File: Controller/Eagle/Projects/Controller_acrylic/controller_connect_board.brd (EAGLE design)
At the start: 280.8 x 115 mm, 17 parts, among them J1 GIMBAL_3PIN, J2 GIMBAL_3PIN, J3 GIMBAL_3PIN, J4 GIMBAL_3PIN

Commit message: Made new eagle project for controller connector board Made new JST connect device that matches the JST connector (not sure why it didn't originally)
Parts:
- added J5: GIMBAL_3PIN_MATCH_TDOCU, Controller:JST-3-PTH
- added JP2: (no value), SparkFun-Connectors:1X01
- J1, J2, J3, J4: value GIMBAL_3PIN -> GIMBAL_3PIN_MATCH_TDOCU
- R1, R2, R3, R4: value (none) -> 5k
- moved R1 47.7 mm to (108.3, 38.2), turned to 270 degrees
- moved U$3 46.1 mm to (123.9, 114.0), flipped to the top
- moved J4 43.4 mm to (83.0, 49.0), turned to 270 degrees
- moved J2 17.7 mm to (200.0, 28.0)
- moved R3 16.6 mm to (187.4, 33.0), turned to 180 degrees
- moved R2 9.22 mm to (70.9, 37.9)
- moved R4 8.54 mm to (172.6, 40.7)
- moved U$6 8.54 mm to (98.0, 33.0)
- moved U$7 8.54 mm to (153.0, 33.0)
- moved JP1 8.25 mm to (105.0, 52.0), turned to 270 degrees
- moved J1 6.71 mm to (186.0, 51.0)
- moved J3 6.08 mm to (71.0, 49.0)
- moved JP6 2.24 mm to (126.0, 45.0)
- turned U$1 to 180 degrees
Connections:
- new net N$9: J5.3, JP2.1
- net 3.3V: now also J5.1
- net GND: now also J1.2, J2.2, J3.2, J4.2, J5.2; no longer J1.3, J2.3, J3.3, J4.3
- net N$5: now also J1.3; no longer J1.2
- net N$6: now also J2.3; no longer J2.2
- net N$7: now also J3.3; no longer J3.2
- net N$8: now also J4.3; no longer J4.2
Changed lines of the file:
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@@
 <layer number="49" name="Reference" color="7" fill="1" visible="no" active="yes"/>
 <layer number="50" name="dxf" color="7" fill="1" visible="no" active="no"/>
-<layer number="51" name="tDocu" color="7" fill="1" visible="no" active="yes"/>
-<layer number="52" name="bDocu" color="7" fill="1" visible="no" active="yes"/>
+<layer number="51" name="tDocu" color="7" fill="1" visible="yes" active="yes"/>
+<layer number="52" name="bDocu" color="7" fill="1" visible="yes" active="yes"/>
 <layer number="53" name="tGND_GNDA" color="7" fill="1" visible="no" active="no"/>
 <layer number="54" name="bGND_GNDA" color="7" fill="1" visible="no" active="no"/>
@@
 <dimension x1="220" y1="57.5" x2="220" y2="0" x3="206.3" y3="28.75" textsize="1.778" layer="47" visible="yes"/>
 <dimension x1="220" y1="57.5" x2="250" y2="61.6" x3="235" y3="62.85" textsize="1.778" layer="47" dtype="horizontal" visible="yes"/>
+<wire x1="217" y1="22" x2="217" y2="44" width="0.01" layer="20"/>
+<wire x1="217" y1="44" x2="190" y2="44" width="0.01" layer="20"/>
+<wire x1="190" y1="44" x2="190" y2="55" width="0.01" layer="20"/>
+<wire x1="190" y1="55" x2="67" y2="55" width="0.01" layer="20"/>
+<wire x1="67" y1="55" x2="67" y2="42" width="0.01" layer="20"/>
+<wire x1="67" y1="42" x2="32" y2="42" width="0.01" layer="20"/>
+<wire x1="32" y1="42" x2="32" y2="22" width="0.01" layer="20"/>
+<wire x1="32" y1="22" x2="217" y2="22" width="0.01" layer="20"/>
 </plain>
 <attributes>
@@
 </autorouter>
 <elements>
-<element name="U$3" library="BOBs" package="ATMEGA128RFA1" value="" x="170" y="114" rot="MR270"/>
-<element name="U$1" library="Controller" package="GIMBAL_FOOTPRINT" value="" x="29" y="72.5"/>
+<element name="U$3" library="BOBs" package="ATMEGA128RFA1" value="" x="123.883" y="113.963" rot="R270"/>
+<element name="U$1" library="Controller" package="GIMBAL_FOOTPRINT" value="" x="29" y="72.5" rot="R180"/>
 <element name="U$2" library="Controller" package="GIMBAL_FOOTPRINT" value="" x="221" y="72.5"/>
 <element name="U$4" library="Controller" package="SPARKFUN_LCD_33" value="" x="83" y="1"/>
 <element name="U$5" library="Controller" package="CONTROLLER_OUTLINE" value="" x="0" y="0"/>
-<element name="J1" library="Controller" package="JST-3-PTH" value="GIMBAL_3PIN" x="189" y="57" rot="R90"/>
-<element name="J2" library="Controller" package="JST-3-PTH" value="GIMBAL_3PIN" x="213" y="40" rot="R180"/>
-<element name="J3" library="Controller" package="JST-3-PTH" value="GIMBAL_3PIN" x="70" y="55" rot="R270"/>
-<element name="J4" library="Controller" package="JST-3-PTH" value="GIMBAL_3PIN" x="41" y="38" rot="R180"/>
-<element name="R1" library="SparkFun-Resistors" package="1/6W-RES" value="" x="60.780953125" y="42.318003125"/>
-<element name="R2" library="SparkFun-Resistors" package="1/6W-RES" value="" x="72.949403125" y="46.939940625"/>
-<element name="R3" library="SparkFun-Resistors" package="1/6W-RES" value="" x="201.042509375" y="42.352325" rot="R270"/>
-<element name="R4" library="SparkFun-Resistors" package="1/6W-RES" value="" x="175.58266875" y="48.739028125" rot="R270"/>
-<element name="JP6" library="SparkFun-Connectors" package="1X04" value="" x="124" y="46" rot="R90"/>
-<element name="JP1" library="SparkFun-Connectors" package="1X02_NO_SILK" value="" x="113" y="54" rot="R180"/>
-<element name="U$6" library="Components" package="FACEPLATE_MOUNTINGHOLE_M2.5_UNPLATED" value="" x="101" y="41"/>
-<element name="U$7" library="Components" package="FACEPLATE_MOUNTINGHOLE_M2.5_UNPLATED" value="" x="156" y="41"/>
+<element name="J1" library="Controller" package="JST-3-PTH" value="GIMBAL_3PIN_MATCH_TDOCU" x="186" y="51" rot="R90"/>
+<element name="J2" library="Controller" package="JST-3-PTH" value="GIMBAL_3PIN_MATCH_TDOCU" x="200" y="28" rot="R180"/>
+<element name="J3" library="Controller" package="JST-3-PTH" value="GIMBAL_3PIN_MATCH_TDOCU" x="71" y="49" rot="R270"/>
+<element name="J4" library="Controller" package="JST-3-PTH" value="GIMBAL_3PIN_MATCH_TDOCU" x="83" y="49" rot="R270"/>
+<element name="R1" library="SparkFun-Resistors" package="1/6W-RES" value="5k" x="108.318003125" y="38.219046875" rot="R270"/>
+<element name="R2" library="SparkFun-Resistors" package="1/6W-RES" value="5k" x="70.949403125" y="37.939940625"/>
+<element name="R3" library="SparkFun-Resistors" package="1/6W-RES" value="5k" x="187.352325" y="32.957490625" rot="R180"/>
+<element name="R4" library="SparkFun-Resistors" package="1/6W-RES" value="5k" x="172.58266875" y="40.739028125" rot="R270"/>
+<element name="JP6" library="SparkFun-Connectors" package="1X04" value="" x="126" y="45" rot="R90"/>
+<element name="JP1" library="SparkFun-Connectors" package="1X02_NO_SILK" value="" x="105" y="52" rot="R270"/>
+<element name="U$6" library="Components" package="FACEPLATE_MOUNTINGHOLE_M2.5_UNPLATED" value="" x="98" y="33"/>
+<element name="U$7" library="Components" package="FACEPLATE_MOUNTINGHOLE_M2.5_UNPLATED" value="" x="153" y="33"/>
+<element name="J5" library="Controller" package="JST-3-PTH" value="GIMBAL_3PIN_MATCH_TDOCU" x="133" y="29" rot="MR90"/>
+<element name="JP2" library="SparkFun-Connectors" package="1X01" value="" x="169" y="52"/>
 </elements>
 <signals>
 <signal name="GND">
-<contactref element="J4" pad="3"/>
-<contactref element="J1" pad="3"/>
-<contactref element="J2" pad="3"/>
-<contactref element="J3" pad="3"/>
+<contactref element="J4" pad="2"/>
+<contactref element="J1" pad="2"/>
+<contactref element="J2" pad="2"/>
+<contactref element="J3" pad="2"/>
 <contactref element="JP1" pad="1"/>
-<wire x1="211" y1="40" x2="189" y2="59" width="0" layer="19" extent="1-1"/>
-<wire x1="113" y1="54" x2="189" y2="59" width="0" layer="19" extent="1-1"/>
-<wire x1="70" y1="53" x2="113" y2="54" width="0" layer="19" extent="1-1"/>
-<wire x1="39" y1="38" x2="70" y2="53" width="0" layer="19" extent="1-1"/>
+<contactref element="J5" pad="2"/>
+<wire x1="186" y1="51" x2="200" y2="28" width="0" layer="19" extent="1-1"/>
+<wire x1="105" y1="52" x2="186" y2="51" width="0" layer="19" extent="1-1"/>
+<wire x1="71" y1="49" x2="105" y2="52" width="0" layer="19" extent="1-1"/>
+<wire x1="83" y1="49" x2="71" y2="49" width="0" layer="19" extent="1-1"/>
+<wire x1="133" y1="29" x2="83" y2="49" width="0" layer="19" extent="1-1"/>
 </signal>
 <signal name="N$1">
 <contactref element="J4" pad="1"/>
 <contactref element="R1" pad="1"/>
-<wire x1="43" y1="38" x2="58.280953125" y2="42.318003125" width="0" layer="19" extent="1-1"/>
+<wire x1="83" y1="51" x2="108.318003125" y2="40.719046875" width="0" layer="19" extent="1-1"/>
 </signal>
 <signal name="N$2">
 <contactref element="J3" pad="1"/>
 <contactref element="R2" pad="1"/>
-<wire x1="70.449403125" y1="46.939940625" x2="70" y2="57" width="0" layer="19" extent="1-1"/>
+<wire x1="68.449403125" y1="37.939940625" x2="71" y2="51" width="0" layer="19" extent="1-1"/>
 </signal>
 <signal name="N$3">
 <contactref element="J2" pad="1"/>
 <contactref element="R3" pad="1"/>
-<wire x1="201.042509375" y1="44.852325" x2="215" y2="40" width="0" layer="19" extent="1-1"/>
+<wire x1="189.852325" y1="32.957490625" x2="202" y2="28" width="0" layer="19" extent="1-1"/>
 </signal>
 <signal name="N$4">
 <contactref element="J1" pad="1"/>
 <contactref element="R4" pad="1"/>
-<wire x1="175.58266875" y1="51.239028125" x2="189" y2="55" width="0" layer="19" extent="1-1"/>
+<wire x1="172.58266875" y1="43.239028125" x2="186" y2="49" width="0" layer="19" extent="1-1"/>
 </signal>
 <signal name="3.3V">
@@
 <contactref element="R1" pad="2"/>
 <contactref element="JP1" pad="2"/>
-<wire x1="175.58266875" y1="46.239028125" x2="201.042509375" y2="39.852325" width="0" layer="19" extent="1-1"/>
-<wire x1="110.46" y1="54" x2="175.58266875" y2="46.239028125" width="0" layer="19" extent="1-1"/>
-<wire x1="75.449403125" y1="46.939940625" x2="110.46" y2="54" width="0" layer="19" extent="1-1"/>
-<wire x1="63.280953125" y1="42.318003125" x2="75.449403125" y2="46.939940625" width="0" layer="19" extent="1-1"/>
+<contactref element="J5" pad="1"/>
+<wire x1="172.58266875" y1="38.239028125" x2="184.852325" y2="32.957490625" width="0" layer="19" extent="1-1"/>
+<wire x1="105" y1="49.46" x2="172.58266875" y2="38.239028125" width="0" layer="19" extent="1-1"/>
+<wire x1="73.449403125" y1="37.939940625" x2="105" y2="49.46" width="0" layer="19" extent="1-1"/>
+<wire x1="108.318003125" y1="35.719046875" x2="73.449403125" y2="37.939940625" width="0" layer="19" extent="1-1"/>
+<wire x1="133" y1="27" x2="108.318003125" y2="35.719046875" width="0" layer="19" extent="1-1"/>
 </signal>
 <signal name="N$5">
-<contactref element="J1" pad="2"/>
+<contactref element="J1" pad="3"/>
 <contactref element="JP6" pad="1"/>
-<wire x1="124" y1="46" x2="189" y2="57" width="0" layer="19" extent="1-1"/>
+<wire x1="126" y1="45" x2="186" y2="53" width="0" layer="19" extent="1-1"/>
 </signal>
 <signal name="N$6">
-<contactref element="J2" pad="2"/>
+<contactref element="J2" pad="3"/>
 <contactref element="JP6" pad="2"/>
-<wire x1="124" y1="48.54" x2="213" y2="40" width="0" layer="19" extent="1-1"/>
+<wire x1="126" y1="47.54" x2="198" y2="28" width="0" layer="19" extent="1-1"/>
 </signal>
 <signal name="N$7">
-<contactref element="J3" pad="2"/>
+<contactref element="J3" pad="3"/>
 <contactref element="JP6" pad="3"/>
-<wire x1="70" y1="55" x2="124" y2="51.08" width="0" layer="19" extent="1-1"/>
+<wire x1="71" y1="47" x2="126" y2="50.08" width="0" layer="19" extent="1-1"/>
 </signal>
 <signal name="N$8">
-<contactref element="J4" pad="2"/>
+<contactref element="J4" pad="3"/>
 <contactref element="JP6" pad="4"/>
-<wire x1="41" y1="38" x2="124" y2="53.62" width="0" layer="19" extent="1-1"/>
+<wire x1="83" y1="47" x2="126" y2="52.62" width="0" layer="19" extent="1-1"/>
+</signal>
+<signal name="N$9">
+<contactref element="J5" pad="3"/>
+<contactref element="JP2" pad="1"/>
+<wire x1="133" y1="31" x2="169" y2="52" width="0" layer="19" extent="1-1"/>
 </signal>
 </signals>

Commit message: Routing and rubouts
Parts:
- removed U$1, U$2: (no value), Controller:GIMBAL_FOOTPRINT
- removed U$3: (no value), BOBs:ATMEGA128RFA1
- removed U$4: (no value), Controller:SPARKFUN_LCD_33
- removed U$5: (no value), Controller:CONTROLLER_OUTLINE
- moved J5 2.00 mm to (133.0, 27.0)
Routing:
- net GND: track 0.00 -> 224.4 mm
- net 3.3V: track 0.00 -> 174.7 mm
- net N$9: track 0.00 -> 89.0 mm
- net N$6: track 0.00 -> 80.1 mm, vias 0 -> 2
- net N$1: track 0.00 -> 72.5 mm
- net N$5: track 0.00 -> 63.5 mm
- net N$7: track 0.00 -> 57.4 mm
- net N$8: track 0.00 -> 45.4 mm
- net N$4: track 0.00 -> 15.8 mm
- net N$3: track 0.00 -> 14.2 mm
- net N$2: track 0.00 -> 14.1 mm
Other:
- board size 280.8 x 115 mm -> 185 x 33 mm

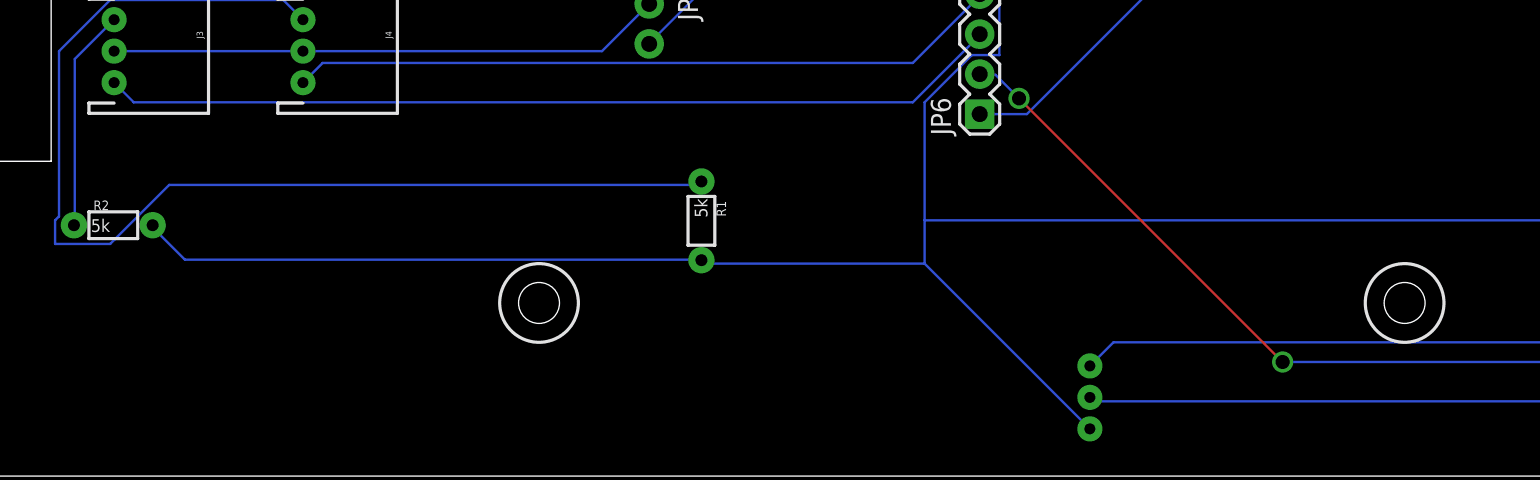
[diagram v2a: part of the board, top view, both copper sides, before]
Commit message: Controller connect board has only the board, no acrylic stuff Added connector board to library so it matches up with acrylic cutouts
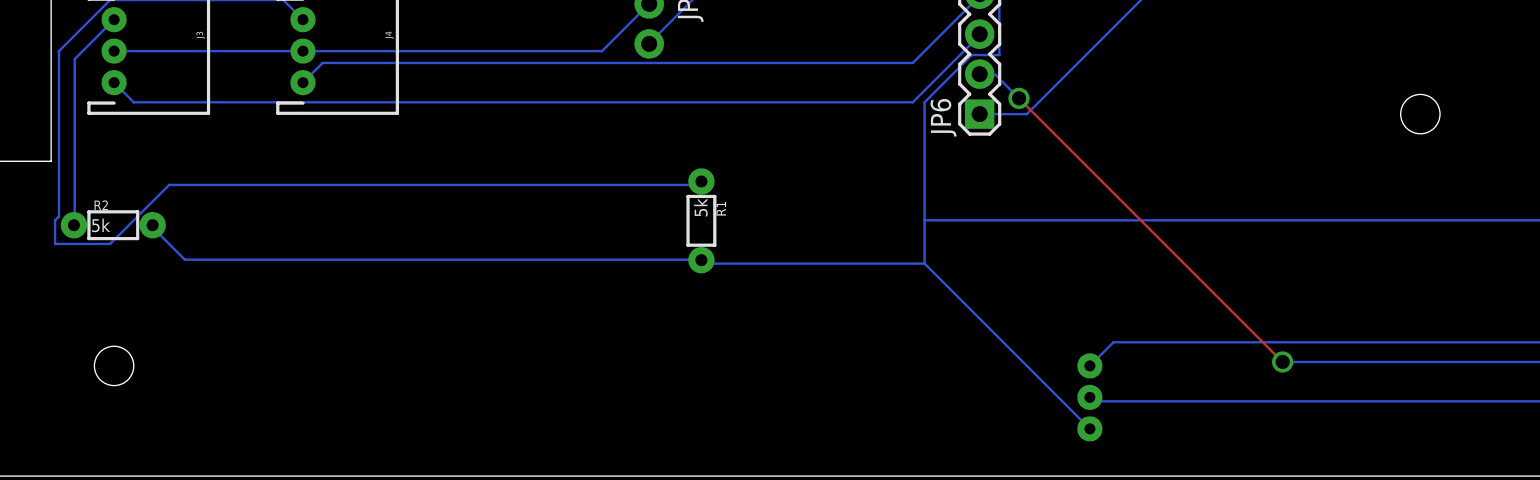
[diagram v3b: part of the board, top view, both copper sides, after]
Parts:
- removed U$6, U$7: (no value), Components:FACEPLATE_MOUNTINGHOLE_M2.5_UNPLATED
- added U$1: (no value), Controller:CONNECTOR_BOARD_OUTLINE
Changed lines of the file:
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@@
 <layer number="26" name="bNames" color="7" fill="1" visible="yes" active="yes"/>
 <layer number="27" name="tValues" color="7" fill="1" visible="yes" active="yes"/>
-<layer number="28" name="bValues" color="7" fill="1" visible="yes" active="yes"/>
+<layer number="28" name="bValues" color="7" fill="1" visible="no" active="yes"/>
 <layer number="29" name="tStop" color="7" fill="3" visible="no" active="yes"/>
 <layer number="30" name="bStop" color="7" fill="6" visible="no" active="yes"/>
@@
 <layer number="160" name="tMountFaceplate" color="11" fill="1" visible="no" active="yes"/>
 <layer number="161" name="bMountFaceplate" color="11" fill="1" visible="no" active="yes"/>
-<layer number="164" name="tRubout" color="13" fill="11" visible="yes" active="yes"/>
-<layer number="165" name="bRubout" color="3" fill="5" visible="yes" active="yes"/>
+<layer number="162" name="tCopperArt" color="7" fill="1" visible="no" active="yes"/>
+<layer number="163" name="bCopperArt" color="7" fill="1" visible="no" active="yes"/>
+<layer number="164" name="tRubout" color="13" fill="11" visible="no" active="yes"/>
+<layer number="165" name="bRubout" color="3" fill="5" visible="no" active="yes"/>
+<layer number="167" name="Fiducials" color="7" fill="1" visible="no" active="yes"/>
 <layer number="199" name="Contour" color="7" fill="1" visible="no" active="yes"/>
 <layer number="200" name="200bmp" color="7" fill="1" visible="no" active="yes"/>
@@
 <dimension x1="220" y1="57.5" x2="220" y2="0" x3="206.3" y3="28.75" textsize="1.778" layer="47" visible="yes"/>
 <dimension x1="220" y1="57.5" x2="250" y2="61.6" x3="235" y3="62.85" textsize="1.778" layer="47" dtype="horizontal" visible="yes"/>
-<wire x1="217" y1="22" x2="217" y2="44" width="0.01" layer="20"/>
-<wire x1="217" y1="44" x2="190" y2="44" width="0.01" layer="20"/>
-<wire x1="190" y1="44" x2="190" y2="55" width="0.01" layer="20"/>
-<wire x1="190" y1="55" x2="67" y2="55" width="0.01" layer="20"/>
-<wire x1="67" y1="55" x2="67" y2="42" width="0.01" layer="20"/>
-<wire x1="67" y1="42" x2="32" y2="42" width="0.01" layer="20"/>
-<wire x1="32" y1="42" x2="32" y2="22" width="0.01" layer="20"/>
-<wire x1="32" y1="22" x2="217" y2="22" width="0.01" layer="20"/>
 <rectangle x1="70" y1="45" x2="72.17" y2="52.12" layer="41"/>
 <rectangle x1="67" y1="36.858" x2="69.517" y2="39" layer="41"/>
@@
 <rectangle x1="126.775" y1="44.641" x2="130.296" y2="47.525" layer="164"/>
 <rectangle x1="143.313" y1="27.499" x2="147.116" y2="30.63" layer="164"/>
+<rectangle x1="126.855" y1="44.693" x2="130.373" y2="47.457" layer="165"/>
 </plain>
 <attributes>
@@
 <element name="JP6" library="SparkFun-Connectors" package="1X04" value="" x="126" y="45" rot="R90"/>
 <element name="JP1" library="SparkFun-Connectors" package="1X02_NO_SILK" value="" x="105" y="52" rot="R270"/>
-<element name="U$6" library="Components" package="FACEPLATE_MOUNTINGHOLE_M2.5_UNPLATED" value="" x="98" y="33"/>
-<element name="U$7" library="Components" package="FACEPLATE_MOUNTINGHOLE_M2.5_UNPLATED" value="" x="153" y="33"/>
 <element name="J5" library="Controller" package="JST-3-PTH" value="GIMBAL_3PIN_MATCH_TDOCU" x="133" y="27" rot="MR90"/>
 <element name="JP2" library="SparkFun-Connectors" package="1X01" value="" x="169" y="52"/>
+<element name="U$1" library="Controller" package="CONNECTOR_BOARD_OUTLINE" value="" x="0" y="0"/>
 </elements>
 <signals>

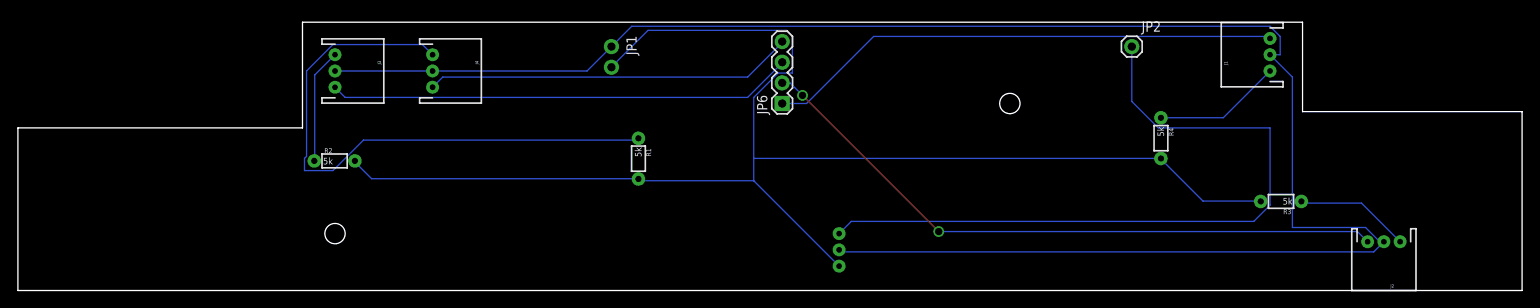
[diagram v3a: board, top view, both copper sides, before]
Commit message: Now it should be ready controller_bottom was not supposed to have the LCD cutout Added dimension to layer 20 in connector board
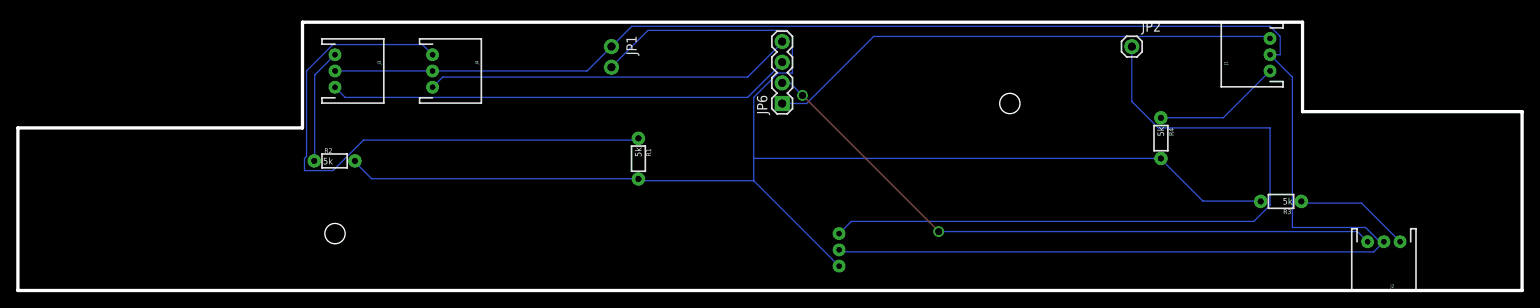
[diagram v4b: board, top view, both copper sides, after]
